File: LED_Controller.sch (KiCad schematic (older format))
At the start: 31 parts, among them CON1 CONNECTOR, CON2 CONNECTOR, CON3 CONNECTOR, CON4 CONNECTOR, CON5 PWR_CON, CON6 AVR-ISP-10, CON7 AVR-ISP-6, IC1 ATMEGA328P-P, Q1 STS8DN3LLH5, Q2 STS8DN3LLH5, Q3 STS8DN3LLH5

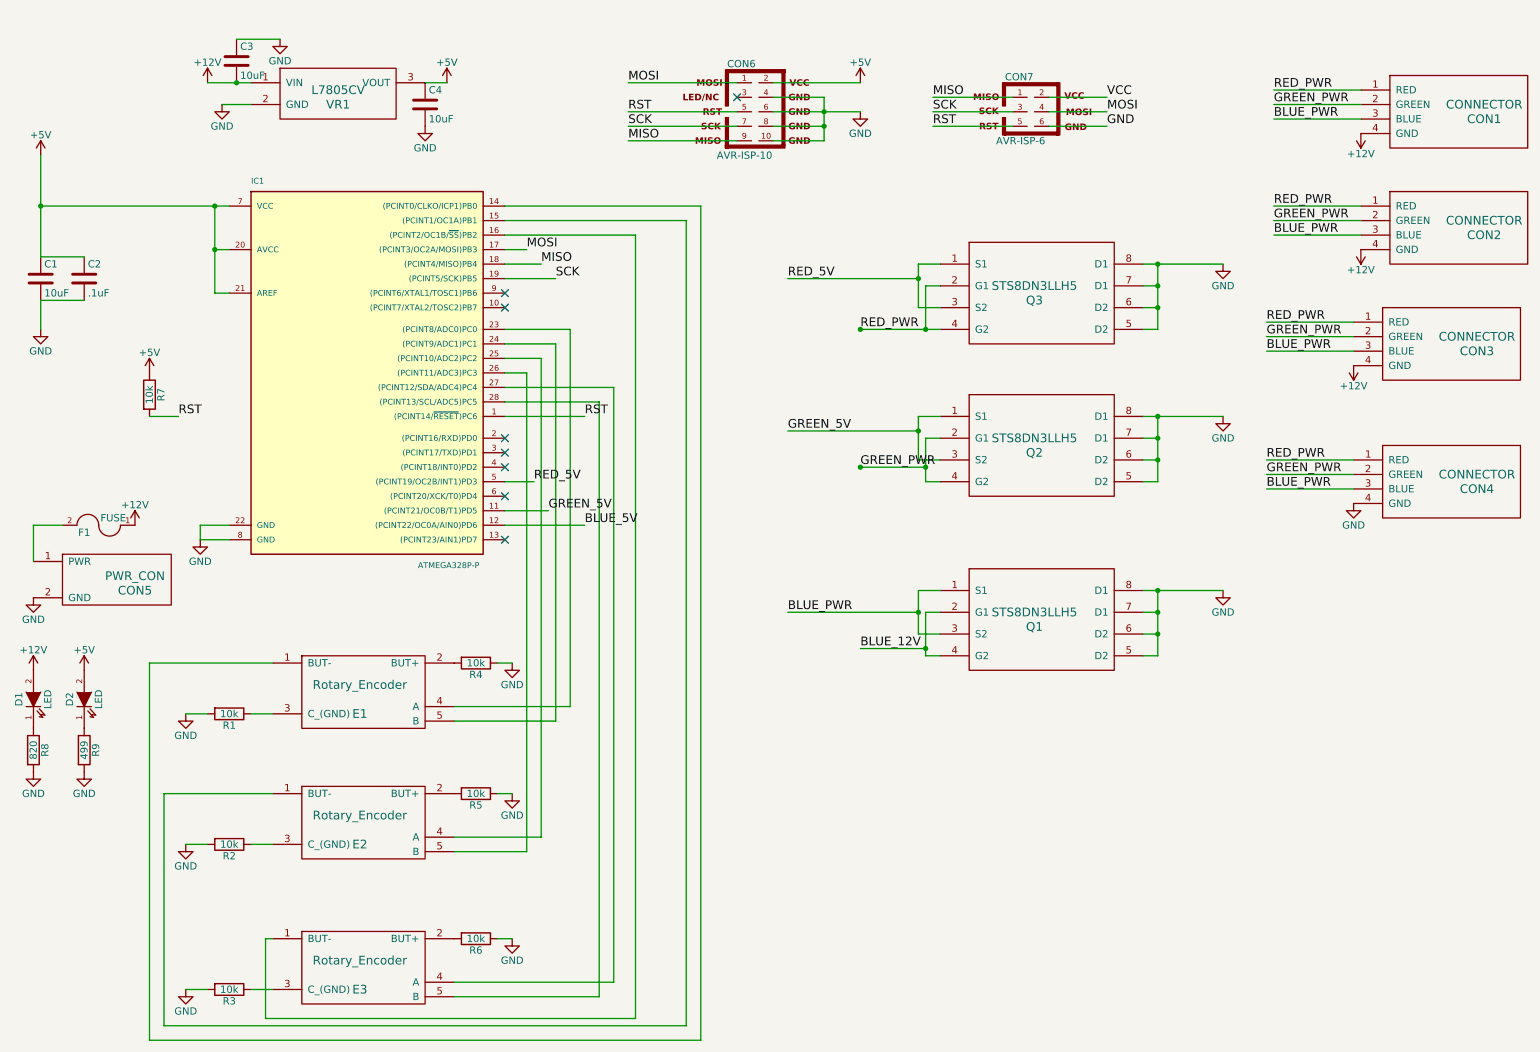
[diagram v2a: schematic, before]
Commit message: Atmega footprint updated, SS Pin changed, Heatsink footprint added
Atmega328p footprint now correct size

Added SS pin for SPI

Made and placed footprint for 50mm square heatsink
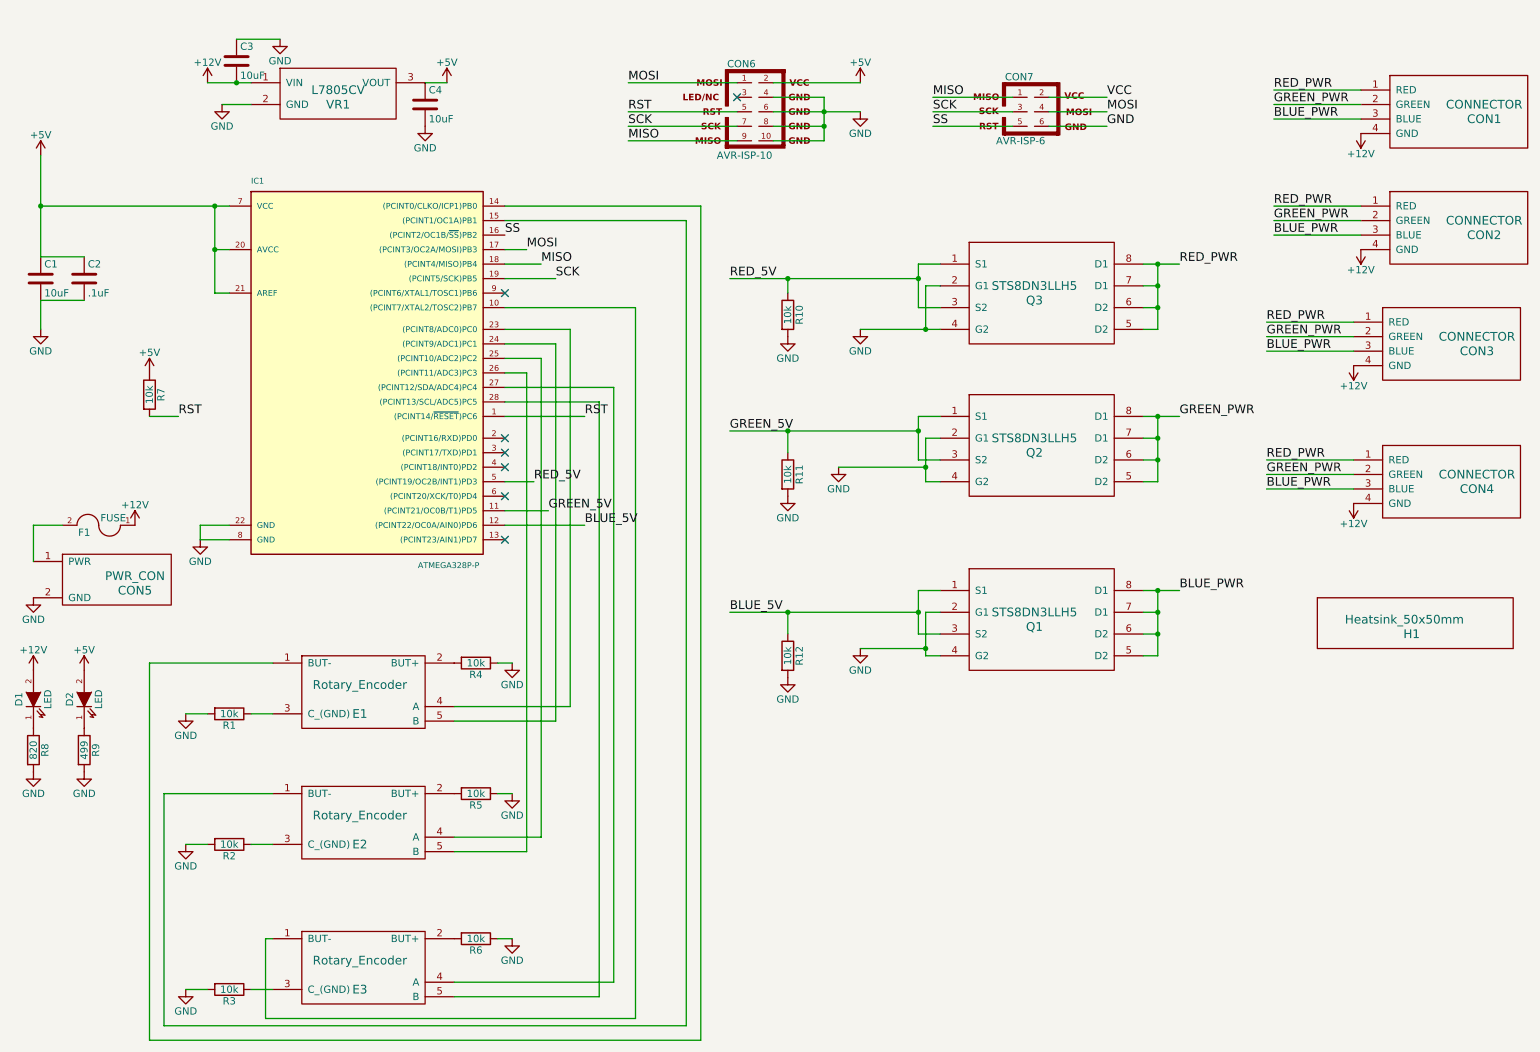
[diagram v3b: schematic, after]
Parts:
- added H1: Heatsink_50x50mm, LED_controller_footprints:Heatsink_50x50mm, symbol Heatsink_50x50mm
- added R10, R11, R12: 10k, LEDs:LED_0603, symbol R
- IC1: footprint Housings_DIP:DIP-28_W15.24mm_LongPads -> Housings_DIP:DIP-28_W7.62mm_LongPads
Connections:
- net BLUE_12V is gone; now on net GND: Q1.2 (G1), Q1.4 (G2)
- net +12V: now also CON4.4 (GND)
- net BLUE_5V: now also Q1.1 (S1), Q1.3 (S2), R12.1
- net BLUE_PWR: now also Q1.5 (D2), Q1.6 (D2), Q1.7 (D1), Q1.8 (D1); no longer Q1.1 (S1), Q1.3 (S2)
- net GND: now also Q2.2 (G1), Q2.4 (G2), Q3.2 (G1), Q3.4 (G2), R10.2, R11.2, R12.2; no longer CON4.4 (GND), Q1.5 (D2), Q1.6 (D2), Q1.7 (D1), Q1.8 (D1), Q2.5 (D2), Q2.6 (D2), Q2.7 (D1), Q2.8 (D1), Q3.5 (D2), Q3.6 (D2), Q3.7 (D1), Q3.8 (D1)
- net GREEN_5V: now also R11.1
- net GREEN_PWR: now also Q2.5 (D2), Q2.6 (D2), Q2.7 (D1), Q2.8 (D1); no longer Q2.2 (G1), Q2.4 (G2)
- net RED_5V: now also R10.1
- net RED_PWR: now also Q3.5 (D2), Q3.6 (D2), Q3.7 (D1), Q3.8 (D1); no longer Q3.2 (G1), Q3.4 (G2)
- net RST: no longer CON7.5
- net at IC1.10 ((PCINT7/XTAL2/TOSC2)PB7): now also E3.1 (BUT-)
- net SS: now reaches IC1.16 ((PCINT2/OC1B/~SS~)PB2)
- net SS: now also CON7.5; no longer E3.1 (BUT-)
- no-connect marks 8 -> 7
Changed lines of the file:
@@
 F 0 "IC1" H 2200 4200 40  0000 L BNN
 F 1 "ATMEGA328P-P" H 3350 1550 40  0000 L BNN
-F 2 "Housings_DIP:DIP-28_W15.24mm_LongPads" H 2950 2950 30  0001 C CIN
+F 2 "Housings_DIP:DIP-28_W7.62mm_LongPads" H 2950 2950 30  0001 C CIN
 F 3 "" H 2950 2950 60  0000 C CNN
 	1    2950 2950
@@
 Text Label 4500 4050 0    60   ~ 0
 BLUE_5V
-Text Label 5900 4650 0    60   ~ 0
-BLUE_PWR
+Text Label 5500 4650 0    60   ~ 0
+BLUE_5V
 Text Label 4250 3950 0    60   ~ 0
 GREEN_5V
 Text Label 4150 3750 0    60   ~ 0
 RED_5V
-Text Label 5900 3400 0    60   ~ 0
+Text Label 5500 3400 0    60   ~ 0
 GREEN_5V
-Text Label 5900 2350 0    60   ~ 0
+Text Label 5500 2350 0    60   ~ 0
 RED_5V
 $Comp
@@
 $EndComp
 NoConn ~ 3950 2450
-NoConn ~ 3950 2550
 NoConn ~ 3950 3450
 NoConn ~ 3950 3550
@@
 	1    0    0    -1
 $EndComp
-$Comp
-L GND #PWR016
-U 1 1 56B7D40D
-P 9800 3900
-F 0 "#PWR016" H 9800 3650 50  0001 C CNN
-F 1 "GND" H 9800 3750 50  0000 C CNN
-F 2 "" H 9800 3900 60  0000 C CNN
-F 3 "" H 9800 3900 60  0000 C CNN
-	1    9800 3900
-	1    0    0    -1
-$EndComp
 Text Label 9200 3600 0    60   ~ 0
 RED_PWR
@@
 Text Label 9200 3800 0    60   ~ 0
 BLUE_PWR
-Text Label 6400 2700 0    60   ~ 0
-RED_PWR
-Text Label 6400 3650 0    60   ~ 0
-GREEN_PWR
-Text Label 6400 4900 0    60   ~ 0
-BLUE_12V
 NoConn ~ 5550 1100
 $Comp
-L GND #PWR017
+L GND #PWR016
 U 1 1 56B801F8
 P 2400 700
-F 0 "#PWR017" H 2400 450 50  0001 C CNN
+F 0 "#PWR016" H 2400 450 50  0001 C CNN
 F 1 "GND" H 2400 550 50  0000 C CNN
 F 2 "" H 2400 700 60  0000 C CNN
@@
 Connection ~ 6800 2350
 Wire Wire Line
-	5900 2350 6800 2350
+	5500 2350 6800 2350
 Wire Wire Line
 	3950 3750 4150 3750
@@
 Connection ~ 6850 4900
 Wire Wire Line
-	6400 3650 6850 3650
-Connection ~ 6400 3650
+	6250 3650 6850 3650
 Connection ~ 6850 3650
 Connection ~ 8450 2250
@@
 	2300 7450 4850 7450
 Wire Wire Line
-	4850 7450 4850 2050
-Wire Wire Line
-	4850 2050 3950 2050
+	4850 7450 4850 2550
+Wire Wire Line
+	4850 2550 3950 2550
 Wire Wire Line
 	3950 1950 5200 1950
@@
 	3950 2350 4300 2350
 Wire Wire Line
-	6800 4650 5900 4650
-Wire Wire Line
-	6800 3400 5900 3400
+	6800 4650 5500 4650
+Wire Wire Line
+	6800 3400 5500 3400
 Wire Wire Line
 	2050 4050 1850 4050
@@
 Wire Wire Line
 	8450 4800 8350 4800
-Connection ~ 6400 2700
 Connection ~ 6850 2700
 Wire Wire Line
@@
 	9800 3800 9200 3800
 Wire Wire Line
-	8350 2250 8900 2250
-Wire Wire Line
-	8350 3300 8900 3300
-Wire Wire Line
-	8350 4500 8900 4500
+	8350 2250 8600 2250
+Wire Wire Line
+	8350 3300 8600 3300
+Wire Wire Line
+	8350 4500 8600 4500
 Wire Wire Line
 	1850 4050 1850 4150
@@
 Text Label 6900 1200 0    60   ~ 0
 SCK
-Text Label 6900 1300 0    60   ~ 0
-RST
 Text Label 8100 1100 0    60   ~ 0
 VCC
@@
 Connection ~ 2100 1000
 $Comp
-L +12V #PWR018
+L +12V #PWR017
 U 1 1 56BAC237
 P 1900 1000
-F 0 "#PWR018" H 1900 850 50  0001 C CNN
+F 0 "#PWR017" H 1900 850 50  0001 C CNN
 F 1 "+12V" H 1900 1140 50  0000 C CNN
 F 2 "" H 1900 1000 60  0000 C CNN
@@
 	700  4050 900  4050
 $Comp
-L +12V #PWR019
+L +12V #PWR018
 U 1 1 56BE5D46
 P 1400 4050
-F 0 "#PWR019" H 1400 3900 50  0001 C CNN
+F 0 "#PWR018" H 1400 3900 50  0001 C CNN
 F 1 "+12V" H 1400 4190 50  0000 C CNN
 F 2 "" H 1400 4050 60  0000 C CNN
@@
 $EndComp
 $Comp
-L +5V #PWR020
+L +5V #PWR019
 U 1 1 56C11944
 P 1500 3000
-F 0 "#PWR020" H 1500 2850 50  0001 C CNN
+F 0 "#PWR019" H 1500 2850 50  0001 C CNN
 F 1 "+5V" H 1500 3140 50  0000 C CNN
 F 2 "" H 1500 3000 60  0000 C CNN
@@
 	1500 3300 1700 3300
 $Comp
-L +12V #PWR021
+L +12V #PWR020
 U 1 1 56C4D7F9
 P 9850 1350
-F 0 "#PWR021" H 9850 1200 50  0001 C CNN
+F 0 "#PWR020" H 9850 1200 50  0001 C CNN
 F 1 "+12V" H 9850 1490 50  0000 C CNN
 F 2 "" H 9850 1350 60  0000 C CNN
@@
 $EndComp
 $Comp
-L +12V #PWR022
+L +12V #PWR021
 U 1 1 56C4D85C
 P 9850 2150
-F 0 "#PWR022" H 9850 2000 50  0001 C CNN
+F 0 "#PWR021" H 9850 2000 50  0001 C CNN
 F 1 "+12V" H 9850 2290 50  0000 C CNN
 F 2 "" H 9850 2150 60  0000 C CNN
@@
 $EndComp
 $Comp
-L +12V #PWR023
+L +12V #PWR022
 U 1 1 56C4D8B8
 P 9800 2950
-F 0 "#PWR023" H 9800 2800 50  0001 C CNN
+F 0 "#PWR022" H 9800 2800 50  0001 C CNN
 F 1 "+12V" H 9800 3090 50  0000 C CNN
 F 2 "" H 9800 2950 60  0000 C CNN
@@
 $EndComp
 $Comp
-L GND #PWR024
-U 1 1 56C4DFDF
-P 8900 2250
-F 0 "#PWR024" H 8900 2000 50  0001 C CNN
-F 1 "GND" H 8900 2100 50  0000 C CNN
-F 2 "" H 8900 2250 60  0000 C CNN
-F 3 "" H 8900 2250 60  0000 C CNN
-	1    8900 2250
-	1    0    0    -1
-$EndComp
-$Comp
-L GND #PWR025
-U 1 1 56C4E044
-P 8900 3300
-F 0 "#PWR025" H 8900 3050 50  0001 C CNN
-F 1 "GND" H 8900 3150 50  0000 C CNN
-F 2 "" H 8900 3300 60  0000 C CNN
-F 3 "" H 8900 3300 60  0000 C CNN
-	1    8900 3300
-	1    0    0    -1
-$EndComp
-$Comp
-L GND #PWR026
-U 1 1 56C4E0A9
-P 8900 4500
-F 0 "#PWR026" H 8900 4250 50  0001 C CNN
-F 1 "GND" H 8900 4350 50  0000 C CNN
-F 2 "" H 8900 4500 60  0000 C CNN
-F 3 "" H 8900 4500 60  0000 C CNN
-	1    8900 4500
-	1    0    0    -1
-$EndComp
-$Comp
-L +12V #PWR027
+L +12V #PWR023
 U 1 1 56C51D4A
 P 700 5050
-F 0 "#PWR027" H 700 4900 50  0001 C CNN
+F 0 "#PWR023" H 700 4900 50  0001 C CNN
 F 1 "+12V" H 700 5190 50  0000 C CNN
 F 2 "" H 700 5050 60  0000 C CNN
@@
 $EndComp
 $Comp
-L GND #PWR028
+L GND #PWR024
 U 1 1 56C5202B
 P 700 5750
-F 0 "#PWR028" H 700 5500 50  0001 C CNN
+F 0 "#PWR024" H 700 5500 50  0001 C CNN
 F 1 "GND" H 700 5600 50  0000 C CNN
 F 2 "" H 700 5750 60  0000 C CNN
@@
 $EndComp
 $Comp
-L +5V #PWR029
+L +5V #PWR025
 U 1 1 56C52093
 P 1050 5050
-F 0 "#PWR029" H 1050 4900 50  0001 C CNN
+F 0 "#PWR025" H 1050 4900 50  0001 C CNN
 F 1 "+5V" H 1050 5190 50  0000 C CNN
 F 2 "" H 1050 5050 60  0000 C CNN
@@
 $EndComp
 $Comp
-L GND #PWR030
+L GND #PWR026
 U 1 1 56C52394
 P 1050 5750
-F 0 "#PWR030" H 1050 5500 50  0001 C CNN
+F 0 "#PWR026" H 1050 5500 50  0001 C CNN
 F 1 "GND" H 1050 5600 50  0000 C CNN
 F 2 "" H 1050 5750 60  0000 C CNN
@@
 Wire Wire Line
 	700  4050 700  4300
+$Comp
+L +12V #PWR027
+U 1 1 56C8C923
+P 9800 3900
+F 0 "#PWR027" H 9800 3750 50  0001 C CNN
+F 1 "+12V" H 9800 4040 50  0000 C CNN
+F 2 "" H 9800 3900 60  0000 C CNN
+F 3 "" H 9800 3900 60  0000 C CNN
+	1    9800 3900
+	-1   0    0    1
+$EndComp
+$Comp
+L GND #PWR028
+U 1 1 56C8D3FD
+P 6400 2700
+F 0 "#PWR028" H 6400 2450 50  0001 C CNN
+F 1 "GND" H 6400 2550 50  0000 C CNN
+F 2 "" H 6400 2700 60  0000 C CNN
+F 3 "" H 6400 2700 60  0000 C CNN
+	1    6400 2700
+	1    0    0    -1
+$EndComp
+$Comp
+L GND #PWR029
+U 1 1 56C8D551
+P 6250 3650
+F 0 "#PWR029" H 6250 3400 50  0001 C CNN
+F 1 "GND" H 6250 3500 50  0000 C CNN
+F 2 "" H 6250 3650 60  0000 C CNN
+F 3 "" H 6250 3650 60  0000 C CNN
+	1    6250 3650
+	1    0    0    -1
+$EndComp
+$Comp
+L GND #PWR030
+U 1 1 56C8D65D
+P 6400 4900
+F 0 "#PWR030" H 6400 4650 50  0001 C CNN
+F 1 "GND" H 6400 4750 50  0000 C CNN
+F 2 "" H 6400 4900 60  0000 C CNN
+F 3 "" H 6400 4900 60  0000 C CNN
+	1    6400 4900
+	1    0    0    -1
+$EndComp
+Text Label 8600 2250 0    60   ~ 0
+RED_PWR
+Text Label 8600 3300 0    60   ~ 0
+GREEN_PWR
+Text Label 8600 4500 0    60   ~ 0
+BLUE_PWR
+Text Label 3950 2050 0    60   ~ 0
+SS
+Text Label 6900 1300 0    60   ~ 0
+SS
+$Comp
+L Heatsink_50x50mm H1
+U 1 1 56C8EFB7
+P 10200 4800
+F 0 "H1" H 10200 4800 60  0000 C CNN
+F 1 "Heatsink_50x50mm" H 10150 4900 60  0000 C CNN
+F 2 "LED_controller_footprints:Heatsink_50x50mm" H 10200 4800 60  0001 C CNN
+F 3 "" H 10200 4800 60  0000 C CNN
+	1    10200 4800
+	1    0    0    -1
+$EndComp
+$Comp
+L R R10
+U 1 1 56C8F742
+P 5900 2600
+F 0 "R10" V 5980 2600 50  0000 C CNN
+F 1 "10k" V 5900 2600 50  0000 C CNN
+F 2 "LEDs:LED_0603" V 5830 2600 30  0001 C CNN
+F 3 "" H 5900 2600 30  0000 C CNN
+	1    5900 2600
+	1    0    0    -1
+$EndComp
+$Comp
+L GND #PWR031
+U 1 1 56C8F951
+P 5900 2750
+F 0 "#PWR031" H 5900 2500 50  0001 C CNN
+F 1 "GND" H 5900 2600 50  0000 C CNN
+F 2 "" H 5900 2750 60  0000 C CNN
+F 3 "" H 5900 2750 60  0000 C CNN
+	1    5900 2750
+	1    0    0    -1
+$EndComp
+$Comp
+L GND #PWR032
+U 1 1 56C8F9CE
+P 5900 3850
+F 0 "#PWR032" H 5900 3600 50  0001 C CNN
+F 1 "GND" H 5900 3700 50  0000 C CNN
+F 2 "" H 5900 3850 60  0000 C CNN
+F 3 "" H 5900 3850 60  0000 C CNN
+	1    5900 3850
+	1    0    0    -1
+$EndComp
+$Comp
+L GND #PWR033
+U 1 1 56C8FA91
+P 5900 5100
+F 0 "#PWR033" H 5900 4850 50  0001 C CNN
+F 1 "GND" H 5900 4950 50  0000 C CNN
+F 2 "" H 5900 5100 60  0000 C CNN
+F 3 "" H 5900 5100 60  0000 C CNN
+	1    5900 5100
+	1    0    0    -1
+$EndComp
+Wire Wire Line
+	5900 4800 5900 4650
+Connection ~ 5900 4650
+Wire Wire Line
+	5900 2450 5900 2350
+Connection ~ 5900 2350
+Wire Wire Line
+	5900 3550 5900 3400
+Connection ~ 5900 3400
+$Comp
+L R R11
+U 1 1 56C902C3
+P 5900 3700
+F 0 "R11" V 5980 3700 50  0000 C CNN
+F 1 "10k" V 5900 3700 50  0000 C CNN
+F 2 "LEDs:LED_0603" V 5830 3700 30  0001 C CNN
+F 3 "" H 5900 3700 30  0000 C CNN
+	1    5900 3700
+	1    0    0    -1
+$EndComp
+$Comp
+L R R12
+U 1 1 56C90346
+P 5900 4950
+F 0 "R12" V 5980 4950 50  0000 C CNN
+F 1 "10k" V 5900 4950 50  0000 C CNN
+F 2 "LEDs:LED_0603" V 5830 4950 30  0001 C CNN
+F 3 "" H 5900 4950 30  0000 C CNN
+	1    5900 4950
+	1    0    0    -1
+$EndComp
 $EndSCHEMATC
